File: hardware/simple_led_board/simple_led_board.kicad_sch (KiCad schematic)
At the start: 2 parts, among them J1 Conn_02x03_Odd_Even

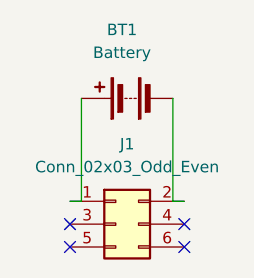
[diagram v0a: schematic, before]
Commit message: Show hardware check issues as tables
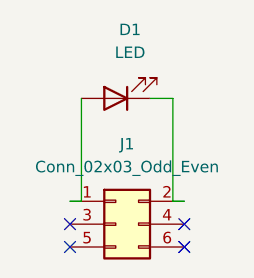
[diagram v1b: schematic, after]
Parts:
- removed BT1: Battery, Battery:BatteryHolder_MYOUNG_BS-07-A1BJ001_CR2032, symbol Device:Battery
- added D1: LED, LED_SMD:LED_0805_2012Metric, symbol Device:LED
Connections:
- net at J1.1 (Pin_1): now also D1.2 (A)
- net at J1.2 (Pin_2): now also D1.1 (K)
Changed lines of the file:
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@@
 	(generator_version "9.0")
 	(paper "A4")
+	(no_connect
+		(at 102.87 76.2)
+	)
+	(no_connect
+		(at 115.57 78.74)
+	)
+	(no_connect
+		(at 115.57 76.2)
+	)
+	(no_connect
+		(at 102.87 78.74)
+	)
 	(wire
 		(pts
@@
 	(wire
 		(pts
+			(xy 111.76 62.23) (xy 114.3 62.23)
+		)
+		(stroke
+			(width 0)
+			(type default)
+		)
+	)
+	(wire
+		(pts
 			(xy 104.14 73.66) (xy 102.87 73.66)
 		)
@@
 			(width 0)
 			(type default)
-		)
-	)
-	(no_connect
-		(at 102.87 76.2)
-	)
-	(no_connect
-		(at 102.87 78.74)
-	)
-	(no_connect
-		(at 115.57 76.2)
-	)
-	(no_connect
-		(at 115.57 78.74)
-	)
-	(symbol
-		(lib_id "Device:Battery")
-		(at 109.22 62.23 90)
-		(unit 1)
-		(exclude_from_sim no)
-		(in_bom yes)
-		(on_board yes)
-		(dnp no)
-		(fields_autoplaced yes)
-		(property "Reference" "BT1"
-			(at 108.6485 54.61 90)
-			(effects
-				(font
-					(size 1.27 1.27)
-				)
-			)
-		)
-		(property "Value" "Battery"
-			(at 108.6485 57.15 90)
-			(effects
-				(font
-					(size 1.27 1.27)
-				)
-			)
-		)
-		(property "Footprint" "Battery:BatteryHolder_MYOUNG_BS-07-A1BJ001_CR2032"
-			(at 107.696 62.23 90)
-			(effects
-				(font
-					(size 1.27 1.27)
-				)
-				(hide yes)
-			)
-		)
-		(property "Datasheet" "~"
-			(at 107.696 62.23 90)
-			(effects
-				(font
-					(size 1.27 1.27)
-				)
-				(hide yes)
-			)
-		)
-		(property "Description" "Multiple-cell battery"
-			(at 109.22 62.23 0)
-			(effects
-				(font
-					(size 1.27 1.27)
-				)
-				(hide yes)
-			)
-		)
-		(pin "1"
-		)
-		(pin "2"
-		)
-		(instances
-			(project ""
-				(path "/3e7d9386-cd47-413a-8a37-d88668a03129"
-					(reference "BT1")
-					(unit 1)
-				)
-			)
 		)
 	)
@@
 					(unit 1)
 				)
+			)
+		)
+	)
+	(symbol
+		(lib_id "Device:LED")
+		(at 107.95 62.23 180)
+		(unit 1)
+		(exclude_from_sim no)
+		(in_bom yes)
+		(on_board yes)
+		(dnp no)
+		(fields_autoplaced yes)
+		(property "Reference" "D1"
+			(at 109.5375 54.61 0)
+			(effects
+				(font
+					(size 1.27 1.27)
+				)
+			)
+		)
+		(property "Value" "LED"
+			(at 109.5375 57.15 0)
+			(effects
+				(font
+					(size 1.27 1.27)
+				)
+			)
+		)
+		(property "Footprint" "LED_SMD:LED_0805_2012Metric"
+			(at 107.95 62.23 0)
+			(effects
+				(font
+					(size 1.27 1.27)
+				)
+				(hide yes)
+			)
+		)
+		(property "Datasheet" "~"
+			(at 107.95 62.23 0)
+			(effects
+				(font
+					(size 1.27 1.27)
+				)
+				(hide yes)
+			)
+		)
+		(property "Description" "Light emitting diode"
+			(at 107.95 62.23 0)
+			(effects
+				(font
+					(size 1.27 1.27)
+				)
+				(hide yes)
+			)
+		)
+		(property "Sim.Pins" "1=K 2=A"
+			(at 107.95 62.23 0)
+			(effects
+				(font
+					(size 1.27 1.27)
+				)
+				(hide yes)
+			)
+		)
+		(pin "1"
+		)
+		(pin "2"
+		)
+		(instances
+			(project ""
+				(path "/3e7d9386-cd47-413a-8a37-d88668a03129"
+					(reference "D1")
+					(unit 1)
+				)
